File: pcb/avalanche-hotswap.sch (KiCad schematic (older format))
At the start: 139 parts, among them J1 TRRS, J3 OLED, P1 i2c_pin, P2 i2c_pin, SW1 SW_Push, SW10 SW_Push, SW11 SW_Push, SW12 SW_Push, SW13 SW_Push, SW14 SW_Push, SW15 SW_Push, SW16 SW_Push, SW17 SW_Push, SW18 SW_Push, SW19 SW_Push, SW2 SW_Push, SW20 SW_Push, SW21 SW_Push, SW22 SW_Push, SW23 SW_Push, SW24 SW_Push, SW25 SW_Push, SW26 SW_Push, SW27 SW_Push, SW28 SW_Push, SW29 SW_Push, SW3 SW_Push, SW30 SW_Push, SW31 SW_Push, SW32 SW_Push, SW33 SW_Push, SW4 SW_Push, SW5 SW_Push, SW6 SW_Push, SW7 SW_Push, SW8 SW_Push, SW9 SW_Push, U1 ProMicro

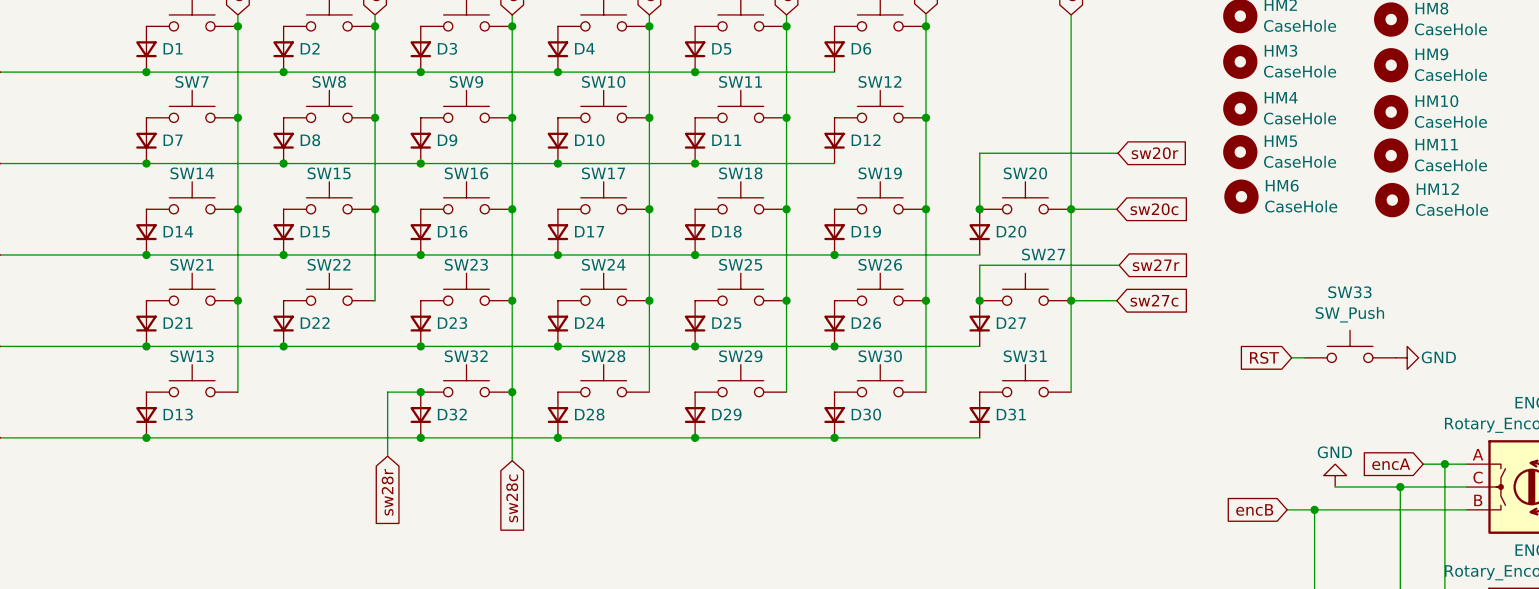
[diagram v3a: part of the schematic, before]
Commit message: Renumbered switches
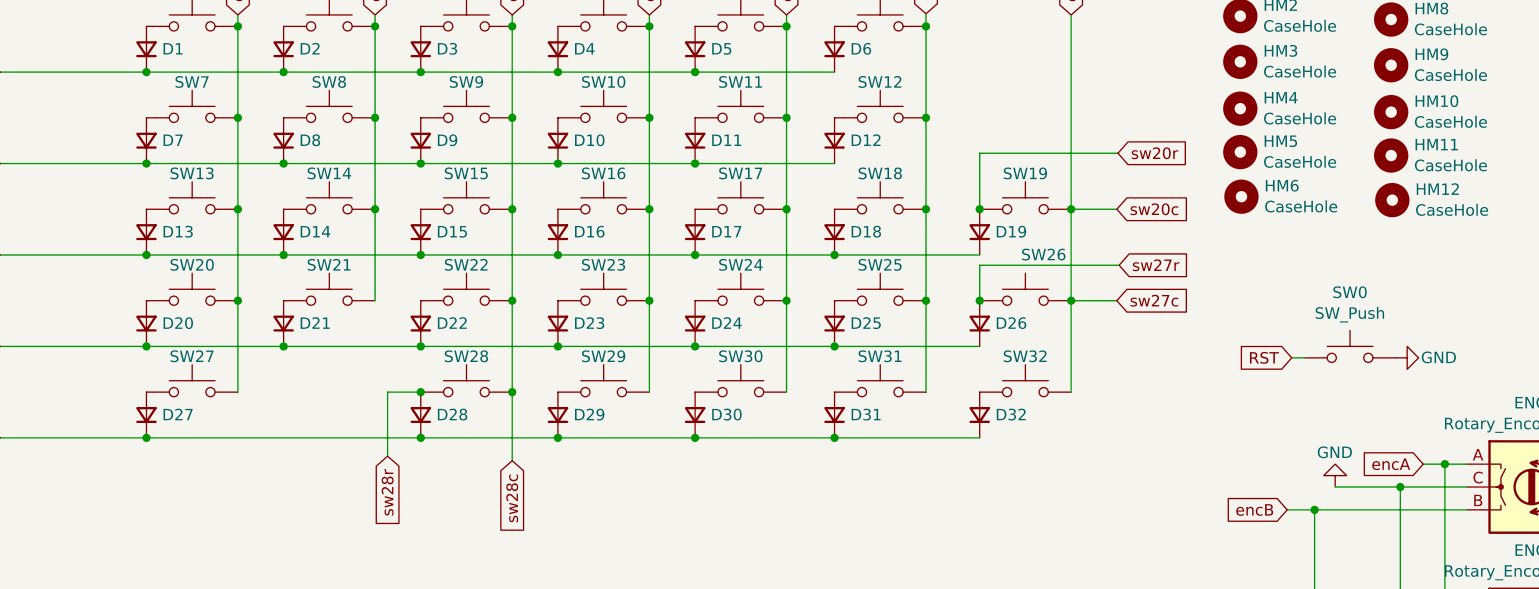
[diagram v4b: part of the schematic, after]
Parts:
- renumbered D14 to D13, D15 to D14, D16 to D15, D17 to D16, D18 to D17, D19 to D18, D20 to D19, D21 to D20, D22 to D21, D23 to D22, D24 to D23, D25 to D24, D26 to D25, D27 to D26, D13 to D27, D32 to D28, D28 to D29, D29 to D30, D30 to D31, D31 to D32, SW33 to SW0, SW14 to SW13, SW15 to SW14, SW16 to SW15, SW17 to SW16, SW18 to SW17, SW19 to SW18, SW20 to SW19, SW21 to SW20, SW22 to SW21, SW23 to SW22, SW24 to SW23, SW25 to SW24, SW26 to SW25, SW27 to SW26, SW13 to SW27, SW32 to SW28, SW28 to SW29, SW29 to SW30, SW30 to SW31, SW31 to SW32

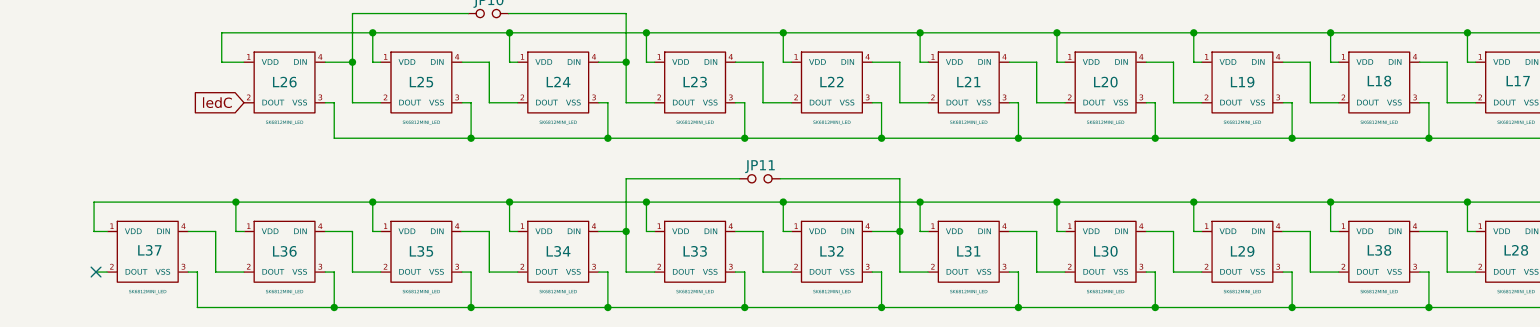
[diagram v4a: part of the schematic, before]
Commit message: Renumbered LEDs
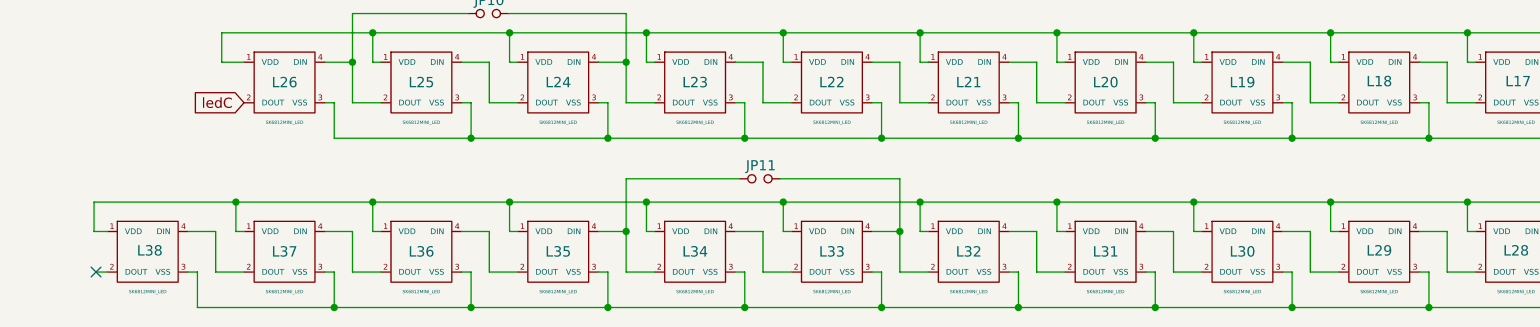
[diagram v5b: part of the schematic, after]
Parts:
- renumbered L38 to L29, L29 to L30, L30 to L31, L31 to L32, L32 to L33, L33 to L34, L34 to L35, L35 to L36, L36 to L37, L37 to L38
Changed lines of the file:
@@
 $EndComp
 $Comp
-L avalanche-hotswap:SK6812MINI_LED L29
+L avalanche-hotswap:SK6812MINI_LED L30
 U 1 1 614A7684
 P 6535 6230
-F 0 "L29" H 6535 6230 51  0000 C CNN
+F 0 "L30" H 6535 6230 51  0000 C CNN
 F 1 "SK6812MINI_LED" H 6535 6033 16  0000 C CNN
 F 2 "used_footprints:YS-SK6812MINI-E" H 6535 6230 60  0001 C CNN
@@
 $EndComp
 $Comp
-L avalanche-hotswap:SK6812MINI_LED L30
+L avalanche-hotswap:SK6812MINI_LED L31
 U 1 1 614A76A9
 P 5860 6230
-F 0 "L30" H 5860 6230 51  0000 C CNN
+F 0 "L31" H 5860 6230 51  0000 C CNN
 F 1 "SK6812MINI_LED" H 5860 6033 16  0000 C CNN
 F 2 "used_footprints:YS-SK6812MINI-E" H 5860 6230 60  0001 C CNN
@@
 $EndComp
 $Comp
-L avalanche-hotswap:SK6812MINI_LED L31
+L avalanche-hotswap:SK6812MINI_LED L32
 U 1 1 614A76B5
 P 5185 6230
-F 0 "L31" H 5185 6230 51  0000 C CNN
+F 0 "L32" H 5185 6230 51  0000 C CNN
 F 1 "SK6812MINI_LED" H 5185 6033 16  0000 C CNN
 F 2 "used_footprints:YS-SK6812MINI-E" H 5185 6230 60  0001 C CNN
@@
 $EndComp
 $Comp
-L avalanche-hotswap:SK6812MINI_LED L32
+L avalanche-hotswap:SK6812MINI_LED L33
 U 1 1 614A76C1
 P 4510 6230
-F 0 "L32" H 4510 6230 51  0000 C CNN
+F 0 "L33" H 4510 6230 51  0000 C CNN
 F 1 "SK6812MINI_LED" H 4510 6033 16  0000 C CNN
 F 2 "used_footprints:YS-SK6812MINI-E" H 4510 6230 60  0001 C CNN
@@
 $EndComp
 $Comp
-L avalanche-hotswap:SK6812MINI_LED L33
+L avalanche-hotswap:SK6812MINI_LED L34
 U 1 1 614A76CD
 P 3835 6230
-F 0 "L33" H 3835 6230 51  0000 C CNN
+F 0 "L34" H 3835 6230 51  0000 C CNN
 F 1 "SK6812MINI_LED" H 3835 6033 16  0000 C CNN
 F 2 "used_footprints:YS-SK6812MINI-E" H 3835 6230 60  0001 C CNN
@@
 $EndComp
 $Comp
-L avalanche-hotswap:SK6812MINI_LED L34
+L avalanche-hotswap:SK6812MINI_LED L35
 U 1 1 614A76D9
 P 3160 6230
-F 0 "L34" H 3160 6230 51  0000 C CNN
+F 0 "L35" H 3160 6230 51  0000 C CNN
 F 1 "SK6812MINI_LED" H 3160 6033 16  0000 C CNN
 F 2 "used_footprints:YS-SK6812MINI-E" H 3160 6230 60  0001 C CNN
@@
 $EndComp
 $Comp
-L avalanche-hotswap:SK6812MINI_LED L35
+L avalanche-hotswap:SK6812MINI_LED L36
 U 1 1 614A76EB
 P 2485 6230
-F 0 "L35" H 2485 6230 51  0000 C CNN
+F 0 "L36" H 2485 6230 51  0000 C CNN
 F 1 "SK6812MINI_LED" H 2485 6033 16  0000 C CNN
 F 2 "used_footprints:YS-SK6812MINI-E" H 2485 6230 60  0001 C CNN
@@
 $EndComp
 $Comp
-L avalanche-hotswap:SK6812MINI_LED L36
+L avalanche-hotswap:SK6812MINI_LED L37
 U 1 1 614A76F7
 P 1810 6230
-F 0 "L36" H 1810 6230 51  0000 C CNN
+F 0 "L37" H 1810 6230 51  0000 C CNN
 F 1 "SK6812MINI_LED" H 1810 6033 16  0000 C CNN
 F 2 "used_footprints:YS-SK6812MINI-E" H 1810 6230 60  0001 C CNN
@@
 $EndComp
 $Comp
-L avalanche-hotswap:SK6812MINI_LED L37
+L avalanche-hotswap:SK6812MINI_LED L38
 U 1 1 614E2B97
 P 1135 6230
-F 0 "L37" H 1145 6235 51  0000 C CNN
+F 0 "L38" H 1145 6235 51  0000 C CNN
 F 1 "SK6812MINI_LED" H 1135 6033 16  0000 C CNN
 F 2 "used_footprints:YS-SK6812MINI-E" H 1135 6230 60  0001 C CNN
@@
 	7010 6130 6970 6130
 $Comp
-L avalanche-hotswap:SK6812MINI_LED L38
+L avalanche-hotswap:SK6812MINI_LED L29
 U 1 1 60FC11F2
 P 7210 6230
-F 0 "L38" H 7210 6235 51  0000 C CNN
+F 0 "L29" H 7210 6235 51  0000 C CNN
 F 1 "SK6812MINI_LED" H 7210 6033 16  0000 C CNN
 F 2 "used_footprints:YS-SK6812MINI-E" H 7210 6230 60  0001 C CNN

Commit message: Minor changes
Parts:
- added HM13: CaseHole, used_footprints:M2_HOLE_PCB, symbol Mechanical:MountingHole
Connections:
- net sw20r renamed sw19r
- net sw27r renamed sw26r
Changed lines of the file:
@@
 Connection ~ 4545 2090
 Text GLabel 8395 1445 2    50   Input ~ 0
-sw20r
+sw19r
 Text GLabel 8390 1690 2    50   Input ~ 0
-sw20c
+sw19c
 Wire Wire Line
 	8190 1690 8390 1690
 Text GLabel 8390 2090 2    50   Input ~ 0
-sw27c
+sw26c
 Wire Wire Line
 	8190 2090 8390 2090
 Text GLabel 8400 1935 2    50   Input ~ 0
-sw27r
+sw26r
 Text GLabel 10665 4105 2    50   Input ~ 0
 sw28r
@@
 sw28c
 Text GLabel 10670 3650 2    50   Input ~ 0
-sw27c
+sw26c
 Text GLabel 10660 3450 2    50   Input ~ 0
-sw27r
+sw26r
 Text GLabel 10670 2805 2    50   Input ~ 0
-sw20r
+sw19r
 Text GLabel 10680 3005 2    50   Input ~ 0
-sw20c
+sw19c
 Wire Wire Line
 	10520 2805 10670 2805
@@
 Wire Wire Line
 	7455 6505 8130 6505
+$Comp
+L Mechanical:MountingHole HM13
+U 1 1 608FDE4C
+P 10350 675
+F 0 "HM13" H 10450 721 50  0000 L CNN
+F 1 "CaseHole" H 10450 630 50  0000 L CNN
+F 2 "used_footprints:M2_HOLE_PCB" H 10350 675 50  0001 C CNN
+F 3 "~" H 10350 675 50  0001 C CNN
+	1    10350 675
+	1    0    0    -1
+$EndComp
 $EndSCHEMATC

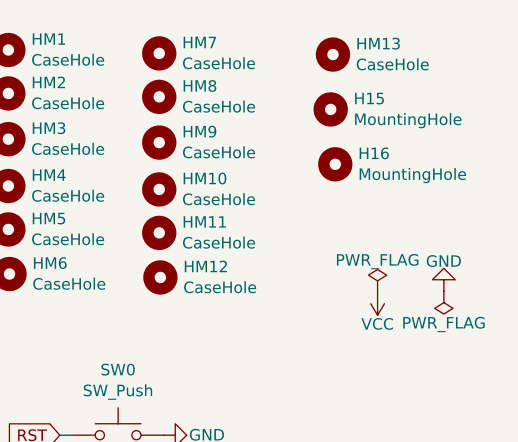
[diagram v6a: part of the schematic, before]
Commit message: Changed holes a bit. Removed old gerbers.
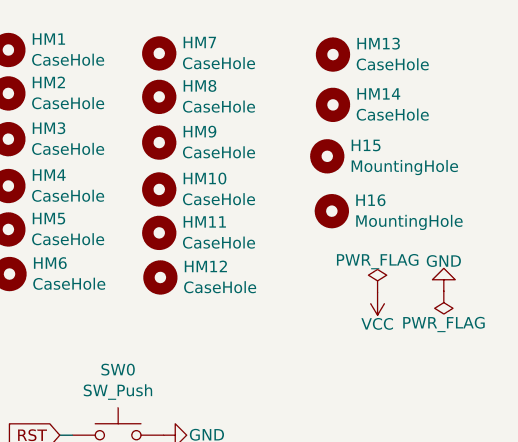
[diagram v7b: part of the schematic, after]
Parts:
- added HM14: CaseHole, used_footprints:M2_HOLE_PCB, symbol Mechanical:MountingHole
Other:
- moved on the sheet: H15, H16
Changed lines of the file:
@@
 L Mechanical:MountingHole H15
 U 1 1 6053584A
-P 10340 915
-F 0 "H15" H 10440 961 50  0000 L CNN
-F 1 "MountingHole" H 10440 870 50  0000 L CNN
-F 2 "used_footprints:M2_HOLE_PCB" H 10340 915 50  0001 C CNN
-F 3 "~" H 10340 915 50  0001 C CNN
-	1    10340 915
+P 10325 1120
+F 0 "H15" H 10425 1166 50  0000 L CNN
+F 1 "MountingHole" H 10425 1075 50  0000 L CNN
+F 2 "used_footprints:M2_HOLE_PCB" H 10325 1120 50  0001 C CNN
+F 3 "~" H 10325 1120 50  0001 C CNN
+	1    10325 1120
 	1    0    0    -1
 $EndComp
@@
 L Mechanical:MountingHole H16
 U 1 1 6044455C
-P 10360 1155
-F 0 "H16" H 10460 1201 50  0000 L CNN
-F 1 "MountingHole" H 10460 1110 50  0000 L CNN
-F 2 "used_footprints:M2_HOLE_PCB" H 10360 1155 50  0001 C CNN
-F 3 "~" H 10360 1155 50  0001 C CNN
-	1    10360 1155
+P 10345 1360
+F 0 "H16" H 10445 1406 50  0000 L CNN
+F 1 "MountingHole" H 10445 1315 50  0000 L CNN
+F 2 "used_footprints:M2_HOLE_PCB" H 10345 1360 50  0001 C CNN
+F 3 "~" H 10345 1360 50  0001 C CNN
+	1    10345 1360
 	1    0    0    -1
 $EndComp
@@
 	1    0    0    -1
 $EndComp
+$Comp
+L Mechanical:MountingHole HM14
+U 1 1 6094ED54
+P 10350 895
+F 0 "HM14" H 10450 941 50  0000 L CNN
+F 1 "CaseHole" H 10450 850 50  0000 L CNN
+F 2 "used_footprints:M2_HOLE_PCB" H 10350 895 50  0001 C CNN
+F 3 "~" H 10350 895 50  0001 C CNN
+	1    10350 895
+	1    0    0    -1
+$EndComp
